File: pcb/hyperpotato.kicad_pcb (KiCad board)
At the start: 2 copper layers, 121.2 x 93 mm, 66 parts, among them J1 Conn_01x02_Socket, J2 Conn_01x02_Socket, J3 Conn_01x04, J4 Conn_01x04, K1 SW_Push, K10 SW_Push, K11 SW_Push, K12 SW_Push, K13 SW_Push, K14 SW_Push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

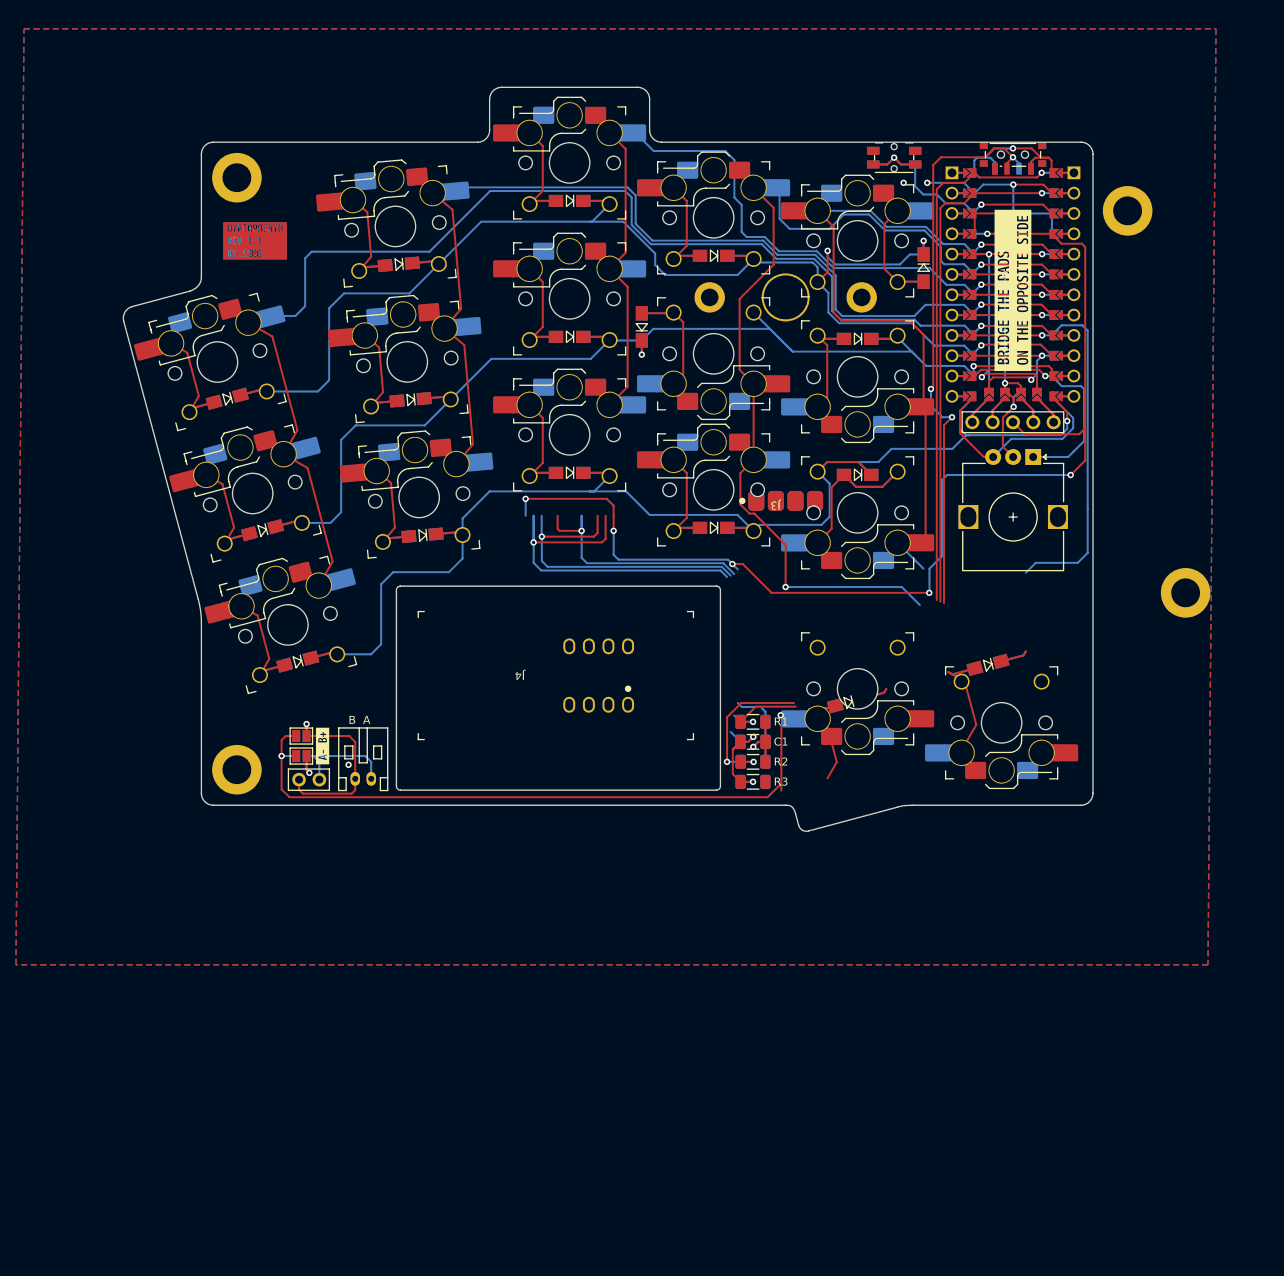
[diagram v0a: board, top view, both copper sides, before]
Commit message: WIP trackpoint mounting
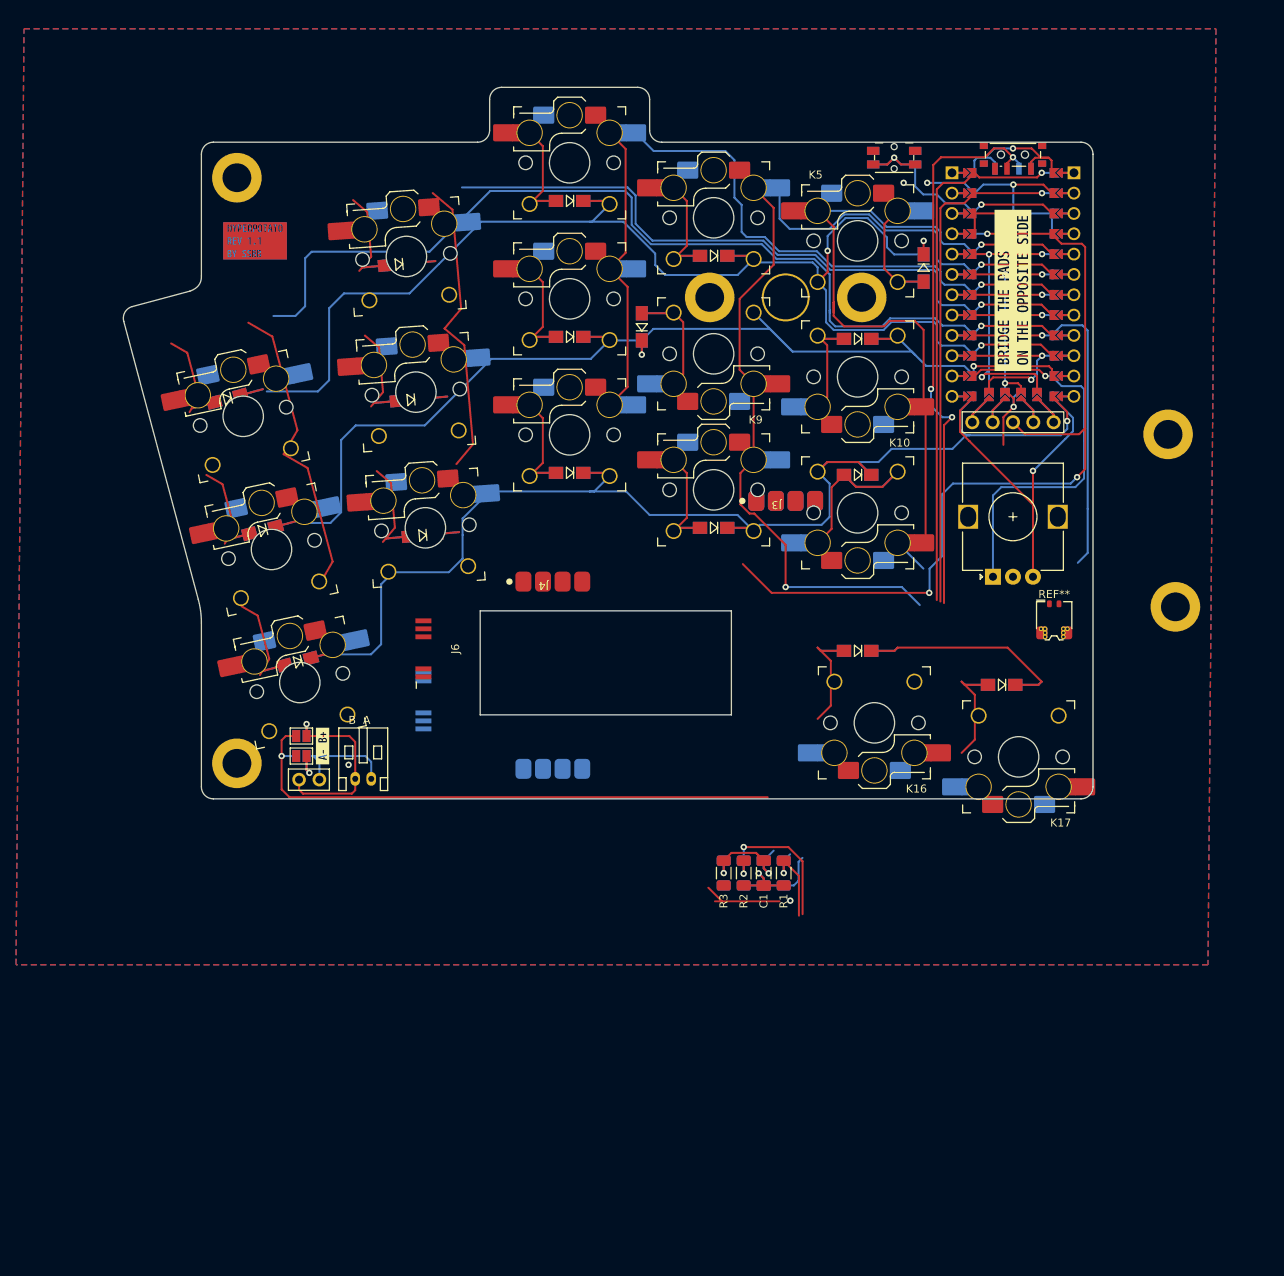
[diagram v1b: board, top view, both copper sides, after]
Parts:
- added J5: Conn_01x04, hyperpotato:Trackpoint_Connector, B.Cu at (100.5, 114.0)
- added J6: Conn_01x12_Socket, hyperpotato:Trackpoint_PCB_Connector, F.Cu at (84.3, 99.1)
- added J7: Conn_01x12_Socket, hyperpotato:Trackpoint_PCB_Connector, B.Cu at (84.3, 105.6)
- added REF**: Molex_Pico-EZmate_78171-0002_1x02-1MP_P1.20mm_Vertical, PCM_marbastlib-various:Molex_Pico-EZmate_78171-0002_1x02-1MP_P1.20mm_Vertical, F.Cu at (163.2, 95.3)
- added REF**: Trackpont_PCB, hyperpotato:Trackpont_PCB, B.Cu at (105.5, 102.3)
- J3: footprint hyperpotato:Trackpoint_Connector -> hyperpotato:Trackpoint_Connector_Reversible
- J4: footprint hyperpotato:Trackponit_PCB -> hyperpotato:Trackpoint_Connector
- TP1: footprint trackpoint_mount_t430 -> hyperpotato:trackpoint_mount_t430
- moved H4 28.4 mm to (177.4, 72.3)
- moved R1 19.3 mm to (129.4, 127.1), turned to -90 degrees
- moved C1 16.5 mm to (126.9, 127.1), turned to 90 degrees
- moved SW3 15.8 mm to (155.5, 90.1), turned to 90 degrees
- moved R2 14.0 mm to (124.4, 127.1), turned to -90 degrees
- moved R3 12.0 mm to (121.9, 127.1), turned to 90 degrees
- moved J4 11.7 mm to (100.5, 90.7), turned to 90 degrees
- moved K1 7.51 mm to (61.8, 70.0), turned to 12 degrees
- moved K6 7.38 mm to (65.3, 86.7), turned to 12 degrees
- moved K11 7.35 mm to (68.9, 103.3), turned to 12 degrees
- moved D16 6.53 mm to (138.6, 99.3), turned to 180 degrees
- moved K17 4.75 mm to (158.7, 112.6)
- moved K16 4.74 mm to (140.7, 108.3)
- moved K2 3.99 mm to (82.2, 50.0), turned to 4 degrees
- moved K7 3.92 mm to (83.4, 67.0), turned to 4 degrees
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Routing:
- net Net-(J3-Pin_1): track 46.2 -> 0.00 mm, vias 1 -> 0
- net TP_PCB_RESET: track 55.1 -> 15.7 mm, vias 3 -> 2
- net VCC: track 165.5 -> 127.9 mm, vias 7 -> 4
- net TP_CLK: track 107.6 -> 75.7 mm, vias 3 -> 2
- net ENC_A: track 28.7 -> 48.6 mm
- net ENC_B: track 27.3 -> 44.1 mm, vias 0 -> 1
- net ROW3: track 65.4 -> 78.1 mm
- net Net-(J3-Pin_2): track 0.00 -> 10.5 mm
- net VBAT: track 153.5 -> 143.0 mm
- net ROW0: track 173.1 -> 178.1 mm
- net GND: track 47.7 -> 45.7 mm
- net COL0: track 158.2 -> 160.2 mm
- net COL1: track 125.2 -> 123.5 mm
- net COL3: track 118.6 -> 119.5 mm
- net COL2: track 103.5 -> 104.2 mm
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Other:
- board size 121.2 x 93 mm -> 121.2 x 88.9 mm

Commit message: Change outlines for the new stagger/splay
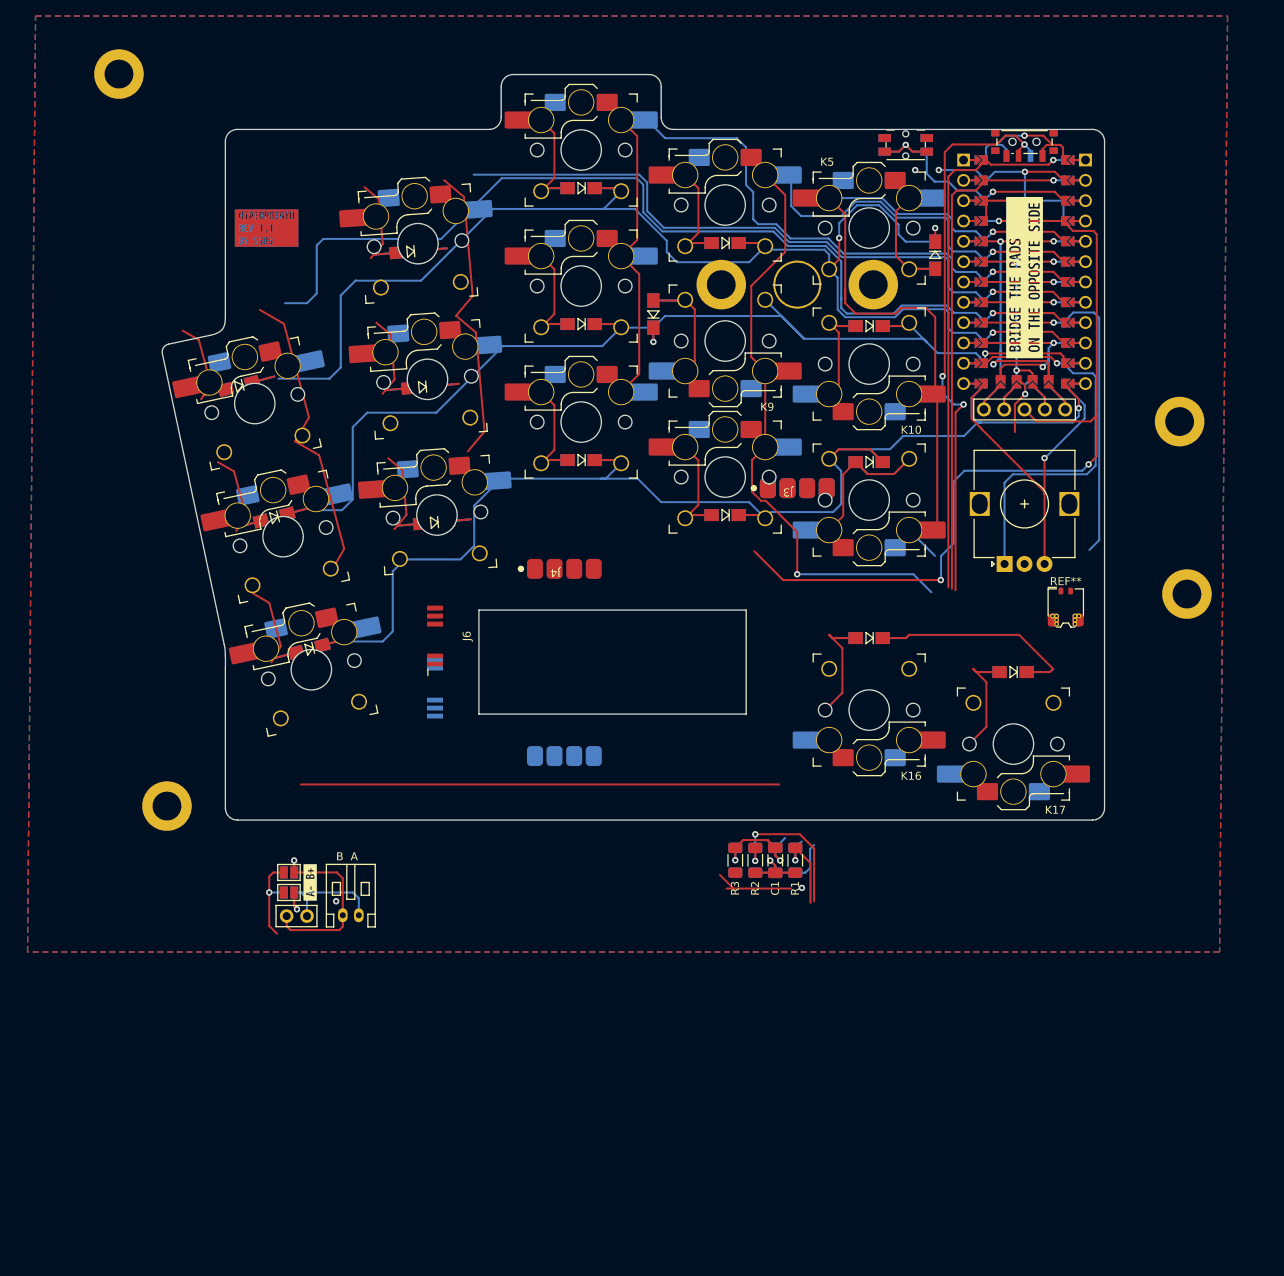
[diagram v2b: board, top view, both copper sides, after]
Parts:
- moved H1 19.6 mm to (46.3, 27.2)
- moved kibuzzard-65B4826D 17.1 mm to (70.2, 128.3)
- moved kibuzzard-65B482C9 17.1 mm to (70.2, 128.3)
- moved JP5 17.1 mm to (67.5, 129.5)
- moved JP6 17.1 mm to (67.5, 129.5)
- moved J2 17.1 mm to (76.3, 132.4)
- moved J1 17.1 mm to (69.8, 132.5)
- moved JP7 17.1 mm to (67.5, 127.0)
- moved JP8 17.1 mm to (67.5, 127.0)
- moved H2 10.2 mm to (52.3, 118.7)
- moved D14 2.15 mm to (122.1, 82.4)
- moved R3 2.15 mm to (123.3, 125.5)
- moved D1 2.15 mm to (61.3, 66.2)
- moved K10 2.15 mm to (140.1, 63.5)
- moved K15 2.15 mm to (140.1, 80.5)
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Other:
- board size 121.2 x 88.9 mm -> 117.8 x 93.2 mm

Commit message: Remove encoder
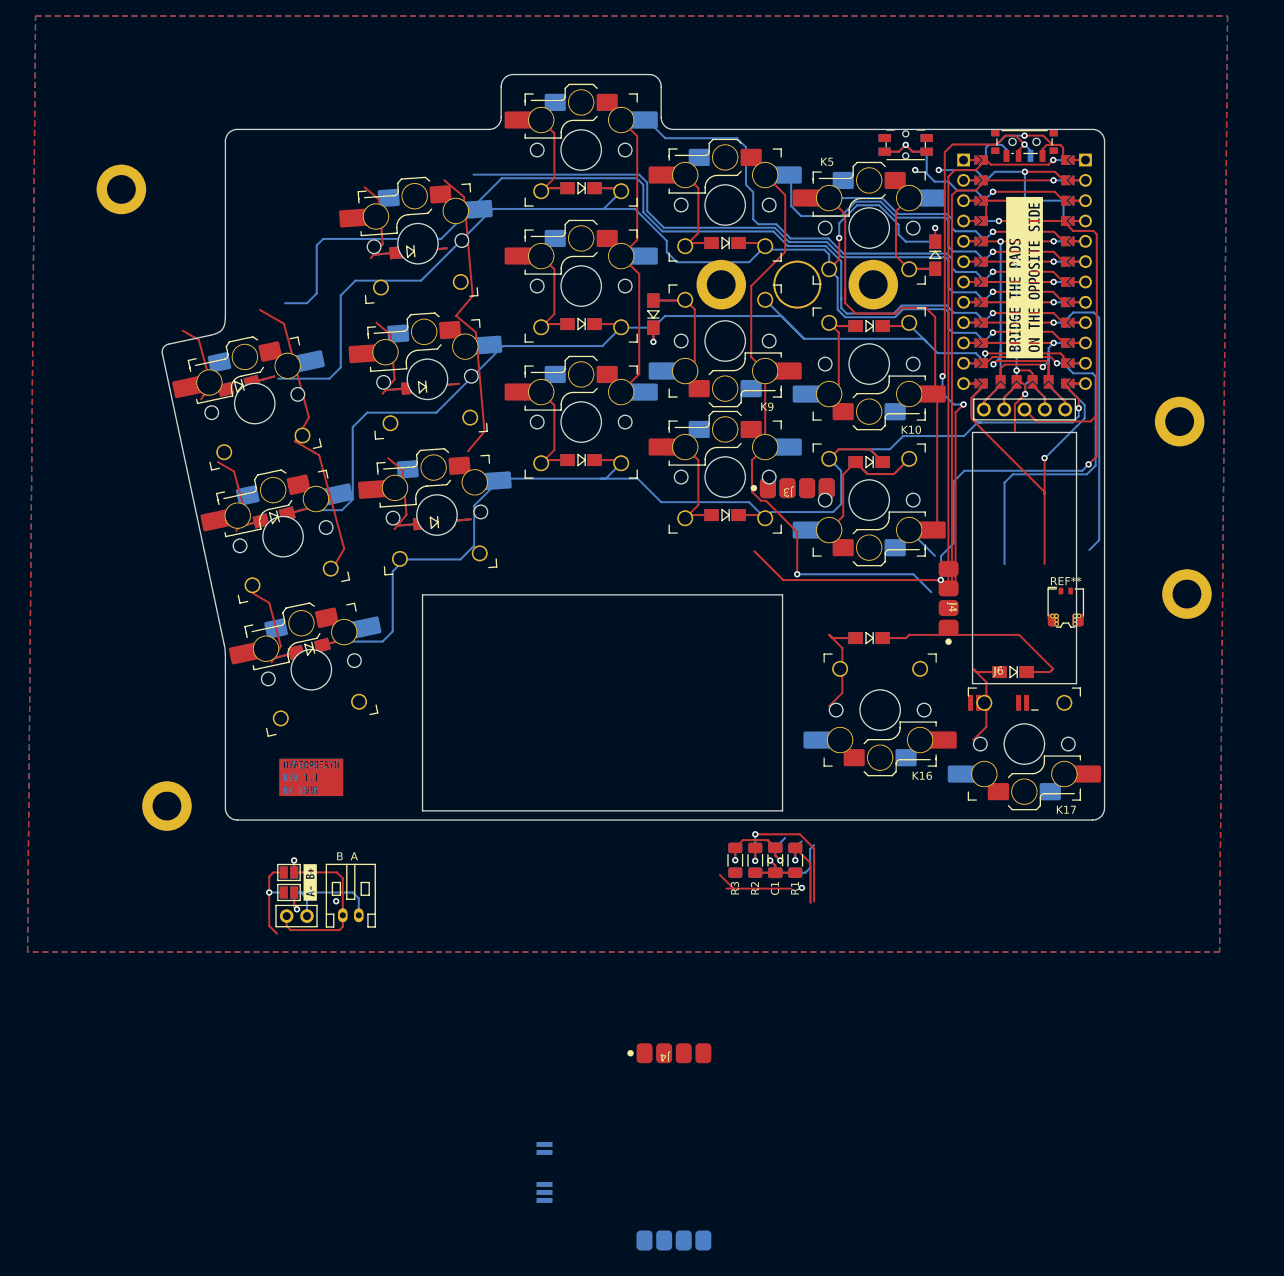
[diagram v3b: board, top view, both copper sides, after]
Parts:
- removed SW3: RotaryEncoder, hyperpotato:RotaryEncoder_Alps_EC12E_Vertical_H20mm
- added J4: Conn_01x04, hyperpotato:Trackpoint_Connector, F.Cu at (150.0, 92.8)
- moved J6 70.9 mm to (156.2, 105.8), turned to 0 degrees
- moved kibuzzard-65CD7866 68.9 mm to (70.3, 115.2)
- moved kibuzzard-65CD786D 68.9 mm to (70.3, 115.2)
- moved J4 62.1 mm to (115.7, 149.7)
- moved J7 62.1 mm to (99.5, 164.5)
- moved J5 62.1 mm to (115.7, 173.0)
- moved REF** 54.1 mm to (159.5, 87.7), turned to 90 degrees
- moved H1 14.4 mm to (46.6, 41.7)
- moved K16 1.37 mm to (141.4, 106.7)
- moved K17 1.37 mm to (159.5, 111.0)
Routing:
- net VBAT: track 143.0 -> 83.2 mm
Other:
- outline, holes or cut-outs redrawn

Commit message: Make outline a bit smaller
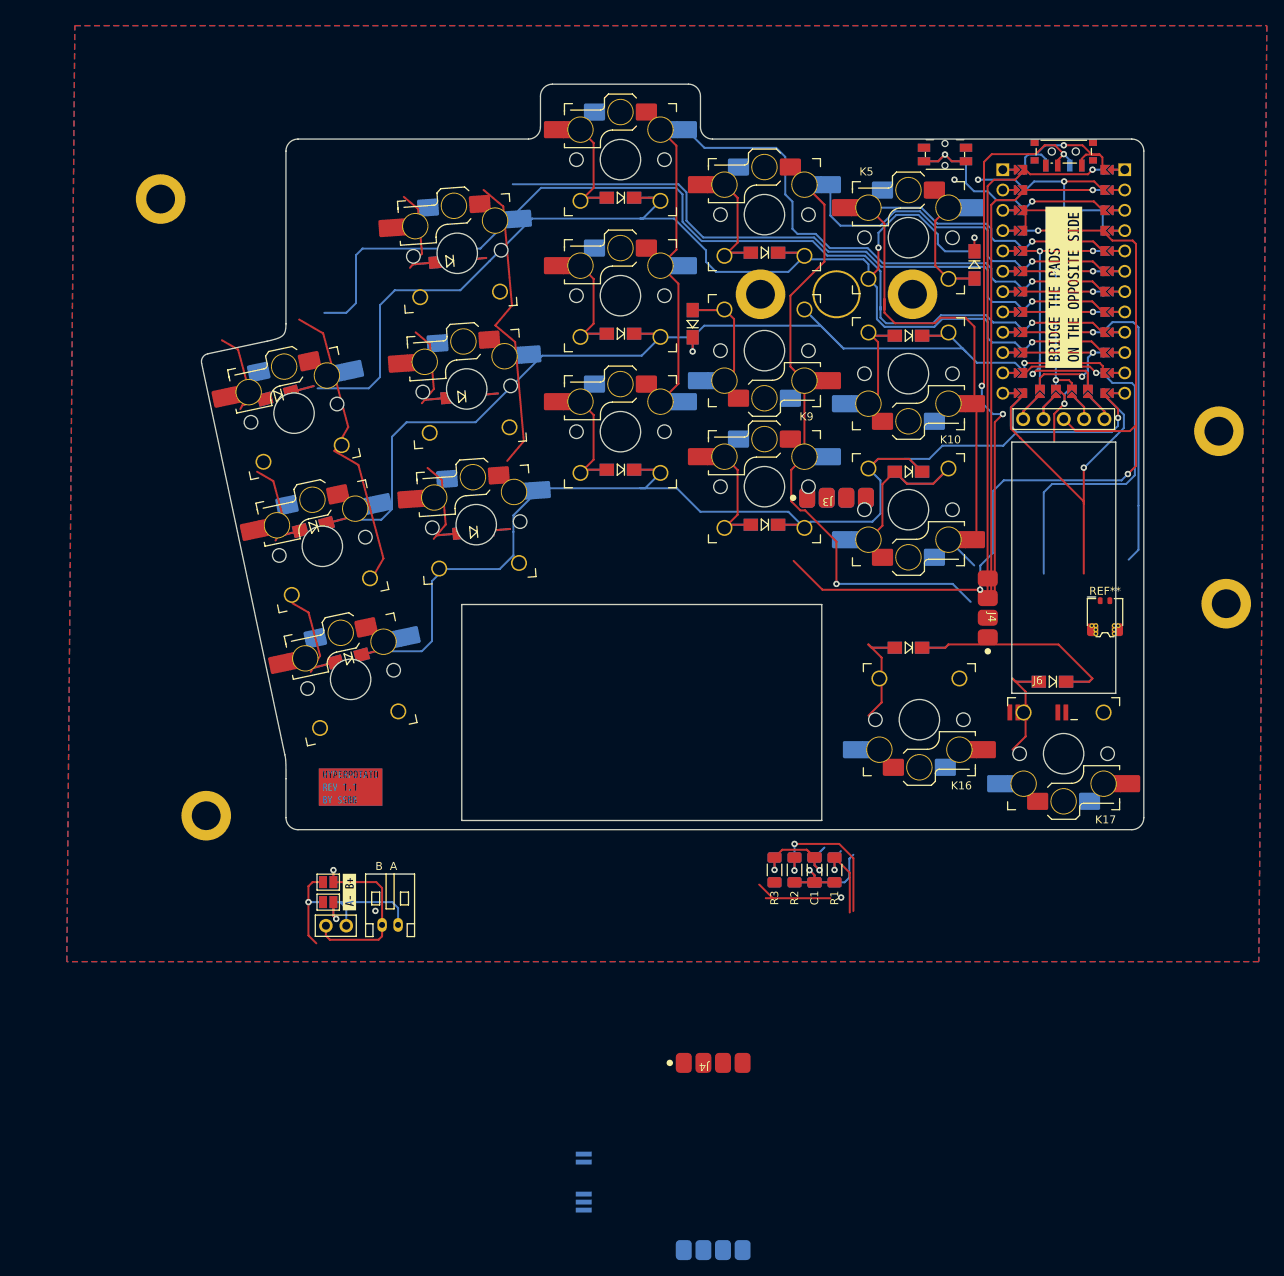
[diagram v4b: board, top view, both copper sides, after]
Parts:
- moved D7 5.05 mm to (89.1, 67.6)
- moved K7 5.05 mm to (89.8, 66.6)
- moved kibuzzard-65CD7866 5.05 mm to (75.2, 116.4)
- moved kibuzzard-65CD786D 5.05 mm to (75.2, 116.4)
- moved J4 5.05 mm to (154.9, 94.0)
- moved K14 5.05 mm to (127.0, 78.8)
- moved H2 5.05 mm to (57.2, 119.9)
- moved D11 5.05 mm to (75.0, 100.3)
- moved J7 5.05 mm to (104.4, 165.7)
- moved JP3 5.05 mm to (165.4, 66.5)
- moved REF** 5.05 mm to (164.4, 88.9)
- moved K4 5.05 mm to (127.0, 44.8)
- moved JP2 5.05 mm to (163.4, 66.5)
- moved J3 5.05 mm to (136.0, 80.3)
- moved R1 5.05 mm to (135.7, 126.7)
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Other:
- outline, holes or cut-outs redrawn
